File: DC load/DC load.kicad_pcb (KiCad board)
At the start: 2 copper layers, 100 x 88.9 mm, 26 parts, among them J1 CTL IN, J2 CTL OUT, J3 B+, J4 B-, M1 3.2mm, M2 3.2mm, M3 3.2mm, Q1 IRFI540, U1 LM324

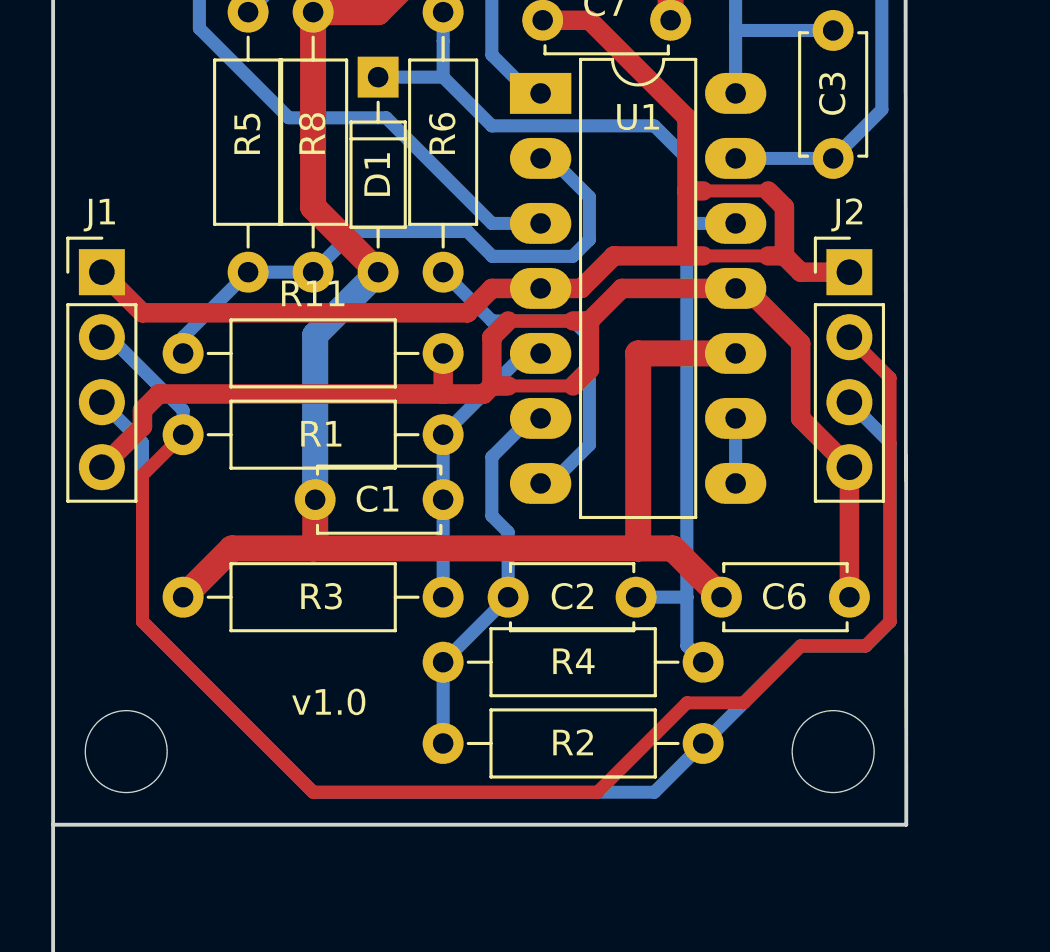
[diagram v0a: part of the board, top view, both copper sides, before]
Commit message: PCB layout - wider power tracks
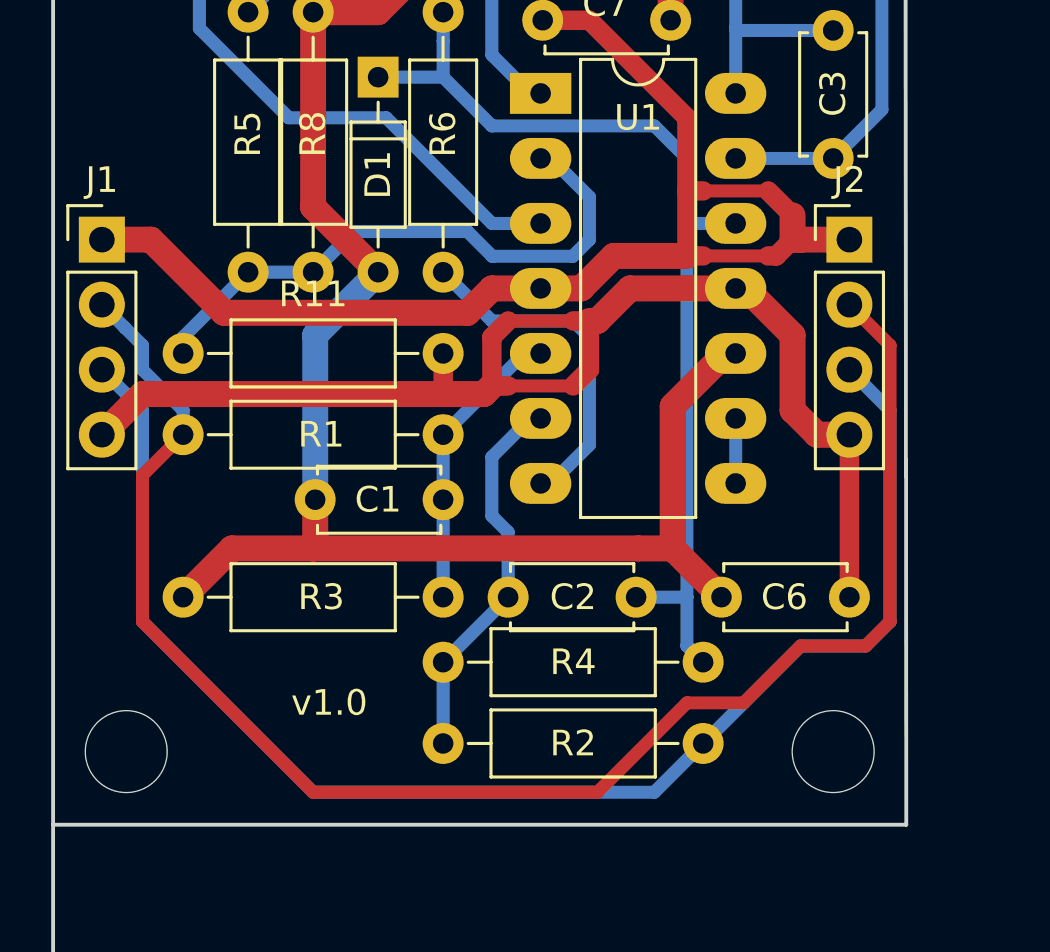
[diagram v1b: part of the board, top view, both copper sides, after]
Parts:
- moved J1 1.27 mm to (35.2, 54.9)
- moved J2 1.27 mm to (64.5, 54.9)
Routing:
- net GND: track 94.9 -> 92.3 mm
- net Net-(J1-Pad3): track 53.2 -> 55.7 mm
- net Net-(J1-Pad2): track 59.8 -> 62.1 mm

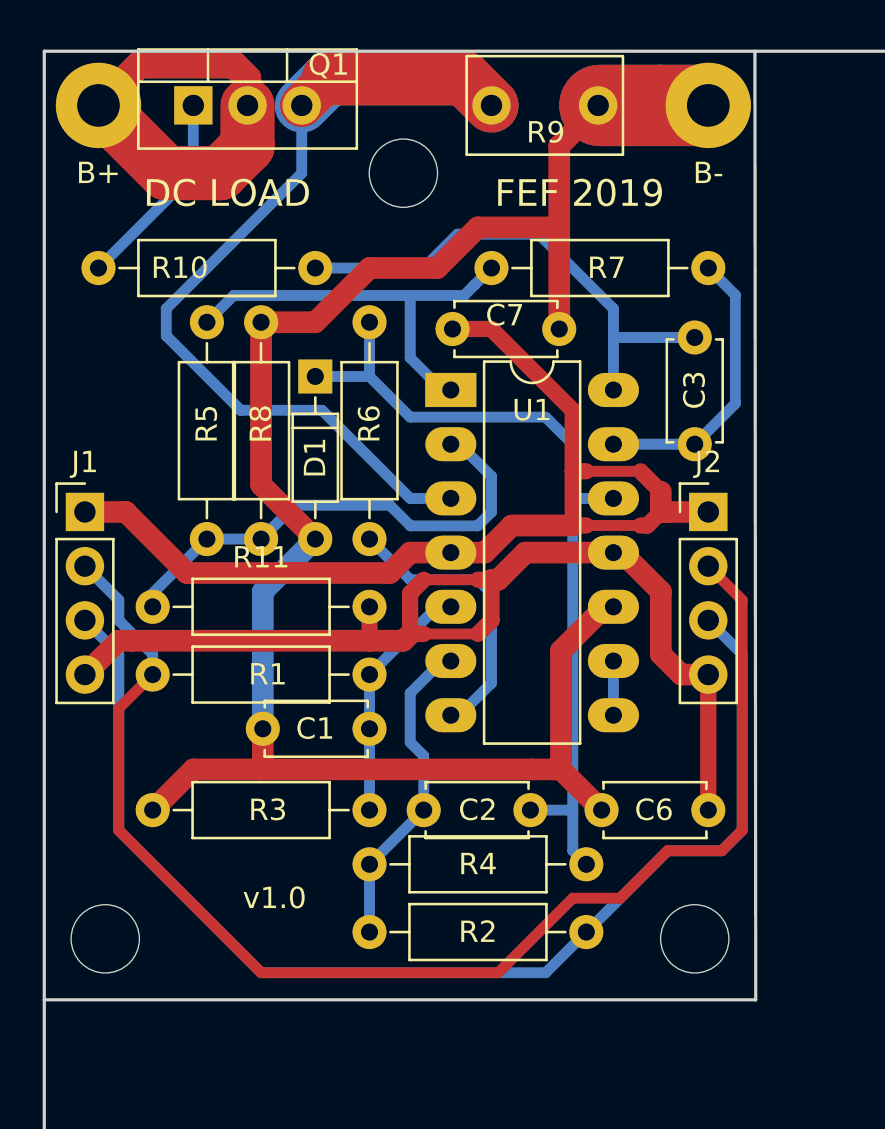
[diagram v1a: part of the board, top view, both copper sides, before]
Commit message: Some layout changes (smaller capacitor outlines; more space for connectors)
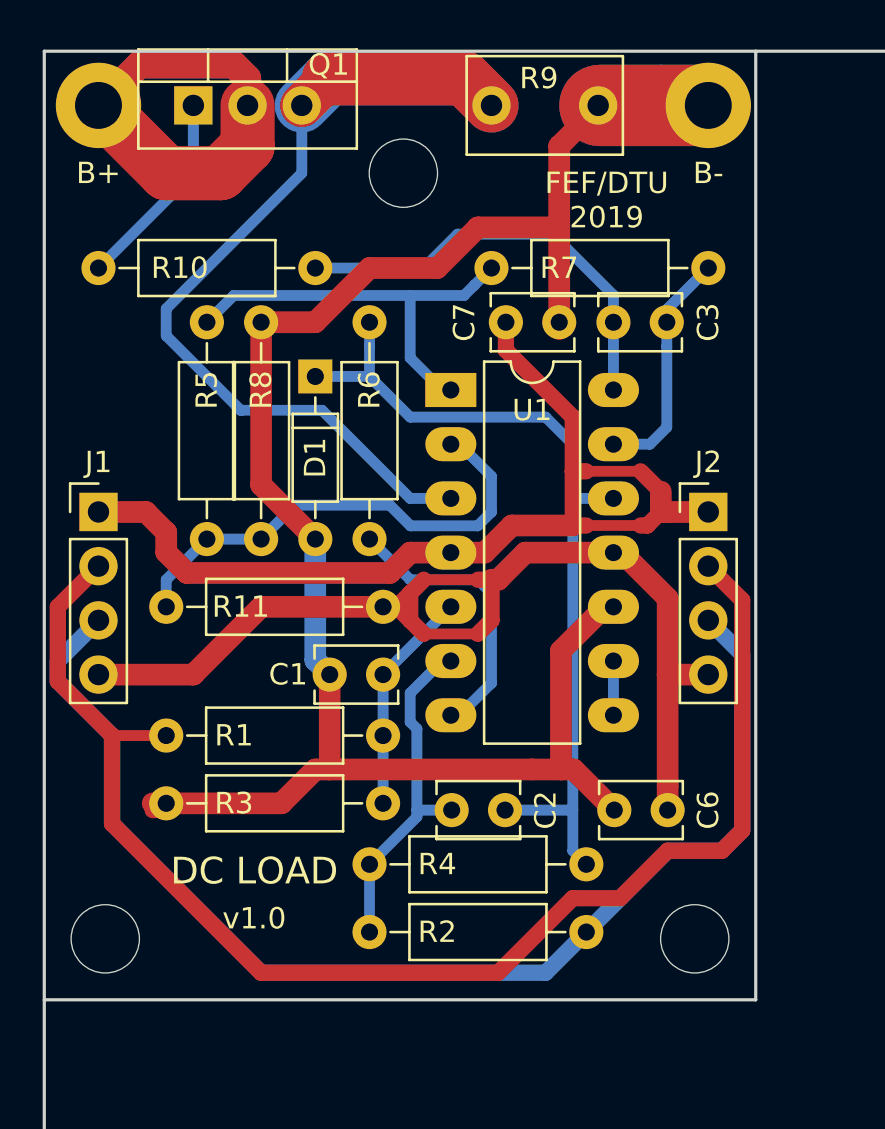
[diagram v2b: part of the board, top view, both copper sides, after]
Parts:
- C1, C2: value 1n -> 10n; footprint Capacitors_THT:C_Disc_D4.7mm_W2.5mm_P5.00mm -> Capacitors_THT:C_Disc_D3.8mm_W2.6mm_P2.50mm
- C3, C6, C7: footprint Capacitors_THT:C_Disc_D4.7mm_W2.5mm_P5.00mm -> Capacitors_THT:C_Disc_D3.8mm_W2.6mm_P2.50mm
- moved C1 4.03 mm to (46.7, 62.5)
- moved C3 3.88 mm to (60.0, 46.0), turned to 0 degrees
- moved R1 2.93 mm to (49.2, 65.4)
- moved C7 2.52 mm to (55.0, 46.0)
- moved C6 1.91 mm to (62.5, 68.9)
- moved C2 1.19 mm to (54.9, 68.9)
- moved R3 0.71 mm to (49.2, 68.6)
- moved R11 0.64 mm to (39.1, 59.4)
- moved J1 0.63 mm to (35.9, 54.9)
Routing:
- net Net-(C3-Pad1): track 23.7 -> 20.3 mm
- net VDD: track 49.7 -> 47.2 mm
- net Net-(C3-Pad2): track 13.4 -> 11.1 mm
- net Net-(J1-Pad2): track 62.1 -> 64.0 mm
- net Net-(C2-Pad2): track 15.0 -> 16.4 mm
- net Net-(J1-Pad3): track 55.7 -> 57.0 mm
- net Net-(C2-Pad1): track 40.2 -> 41.3 mm
- net Net-(C1-Pad2): track 11.5 -> 10.5 mm
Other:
- board text added: "FEF/DTU 2019"
- board text removed: "FEF 2019"

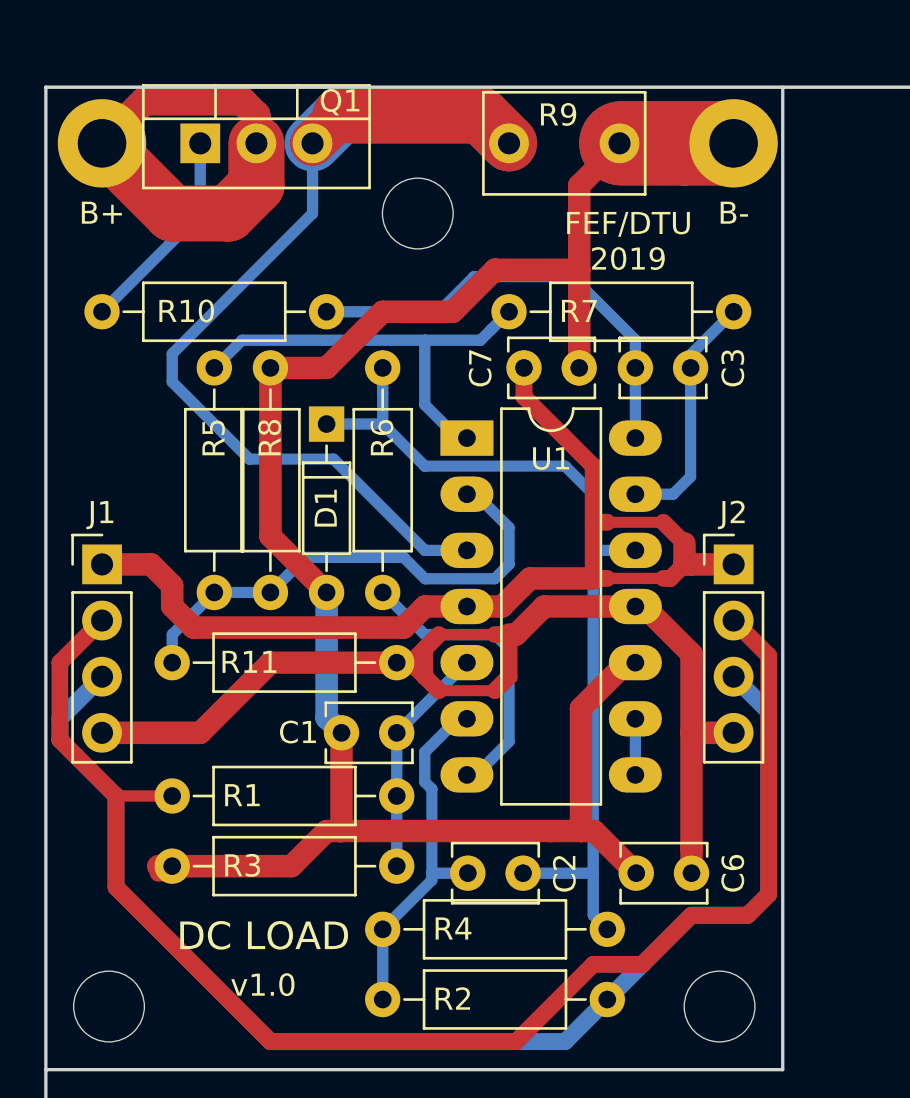
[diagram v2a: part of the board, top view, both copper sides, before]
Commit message: New TO247 housed FET for better dissipation
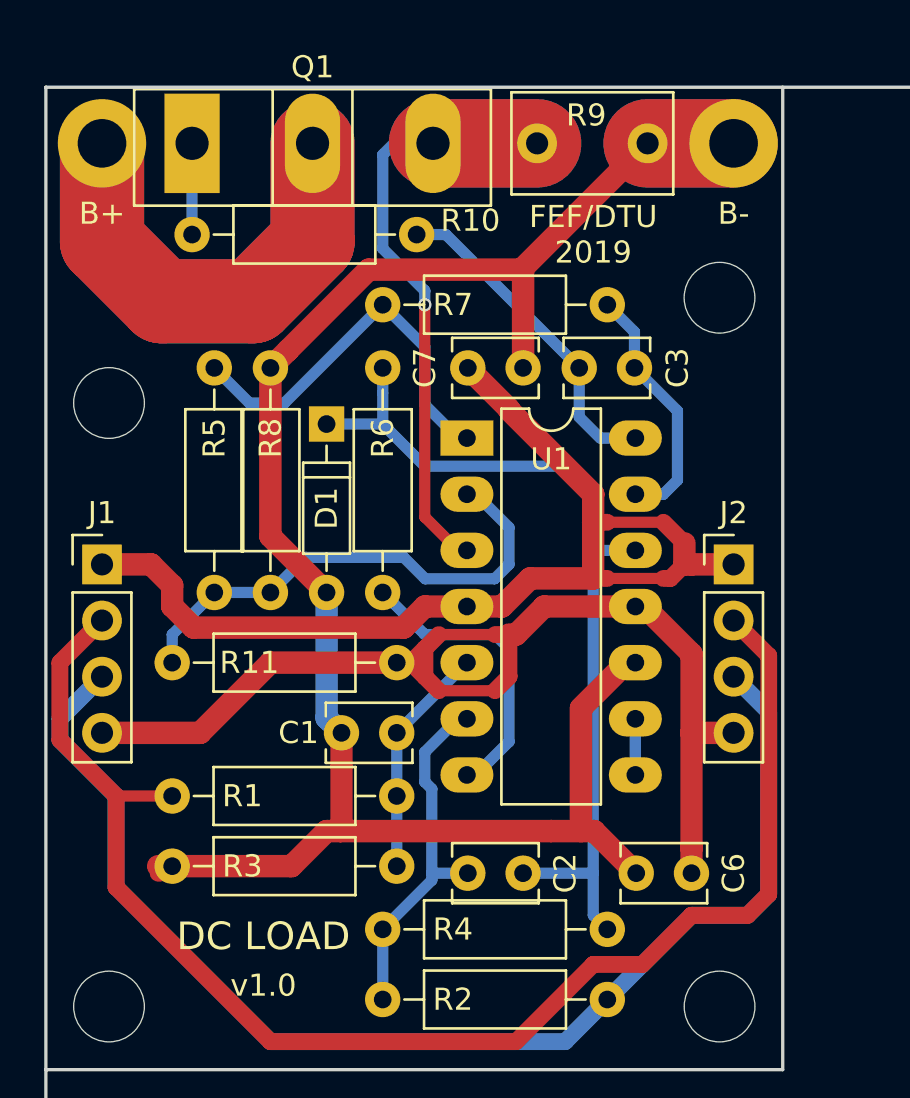
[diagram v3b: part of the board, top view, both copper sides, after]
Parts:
- added M1: 3.2mm, Mounting_Holes:MountingHole_3.2mm_M3_DIN965, F.Cu at (36.2, 47.6)
- Q1: value IRFI540 -> IRFP150NPBF; footprint TO_SOT_Packages_THT:TO-220-3_Vertical -> TO_SOT_Packages_THT:TO-247_TO-3P_Vertical
- moved M1 14.2 mm to (63.8, 42.9)
- moved R7 5.72 mm to (58.7, 43.2)
- moved R10 5.37 mm to (40.0, 40.0)
- moved C3 2.54 mm to (57.5, 46.0)
- moved C7 2.54 mm to (52.4, 46.0)
- moved R9 1.27 mm to (55.6, 35.9)
- moved Q1 0.37 mm to (40.0, 35.9)
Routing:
- net Net-(Q1-Pad3): track 50.2 -> 32.0 mm, vias 0 -> 1
- net Net-(J3-Pad1): track 29.3 -> 41.3 mm
- net Net-(Q1-Pad1): track 9.46 -> 4.13 mm
- net Net-(C3-Pad1): track 20.3 -> 15.0 mm
- net GND: track 92.0 -> 87.9 mm
- net Net-(R5-Pad1): track 20.2 -> 18.4 mm
- net VDD: track 47.2 -> 48.2 mm

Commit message: Layout fixes
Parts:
- renumbered M1 to M4
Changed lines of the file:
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@@
     (links 44)
     (no_connects 0)
-    (area 33.262499 33.262499 133.412501 122.312501)
+    (area 32.919999 31.4525 133.412501 122.312501)
     (thickness 1.6)
     (drawings 23)
@@
   )
   (setup
-    (last_trace_width 3.81)
+    (last_trace_width 0.25)
     (user_trace_width 0.254)
     (user_trace_width 0.381)
@@
     (tags "mounting hole 3.2mm no annular m3 din965")
     (attr virtual)
-    (fp_text reference M1 (at 0 -2.54) (layer F.SilkS) hide
+    (fp_text reference M4 (at 0 -2.54) (layer F.SilkS) hide
       (effects (font (size 1 1) (thickness 0.15)))
     )
@@
     (descr "C, Rect series, Radial, pin pitch=5.00mm, , length*width=7.2*4.5mm^2, Capacitor, http://www.wima.com/EN/WIMA_FKS_2.pdf")
     (tags "C Rect series Radial pin pitch 5.00mm  length 7.2mm width 4.5mm Capacitor")
-    (fp_text reference R9 (at 2.2225 -1.27) (layer F.SilkS)
+    (fp_text reference R9 (at 2.54 -1.5875) (layer F.SilkS)
       (effects (font (size 1 1) (thickness 0.15)))
     )
@@
     (fp_line (start 6.45 2.6) (end 6.45 -2.6) (layer F.CrtYd) (width 0.05))
     (fp_line (start 6.45 -2.6) (end -1.45 -2.6) (layer F.CrtYd) (width 0.05))
-    (fp_text user %R (at 2.2225 -1.27) (layer F.Fab)
+    (fp_text user %R (at 2.54 -1.5875) (layer F.Fab)
       (effects (font (size 1 1) (thickness 0.15)))
     )
@@
     (descr "TO-247, Vertical, RM 5.45mm, TO-3P")
     (tags "TO-247 Vertical RM 5.45mm TO-3P")
-    (fp_text reference Q1 (at 5.45 -3.45) (layer F.SilkS)
+    (fp_text reference Q1 (at 8.625 1.905) (layer F.SilkS)
       (effects (font (size 1 1) (thickness 0.15)))
     )
@@
       (effects (font (size 1 1) (thickness 0.15)))
     )
-    (fp_text user %R (at 5.45 -3.45) (layer F.Fab)
-      (effects (font (size 1 1) (thickness 0.15)))
-    )
+    (fp_text user %R (at 8.625 1.905) (layer F.Fab)
+      (effects (font (size 1 1) (thickness 0.15)))
+    )

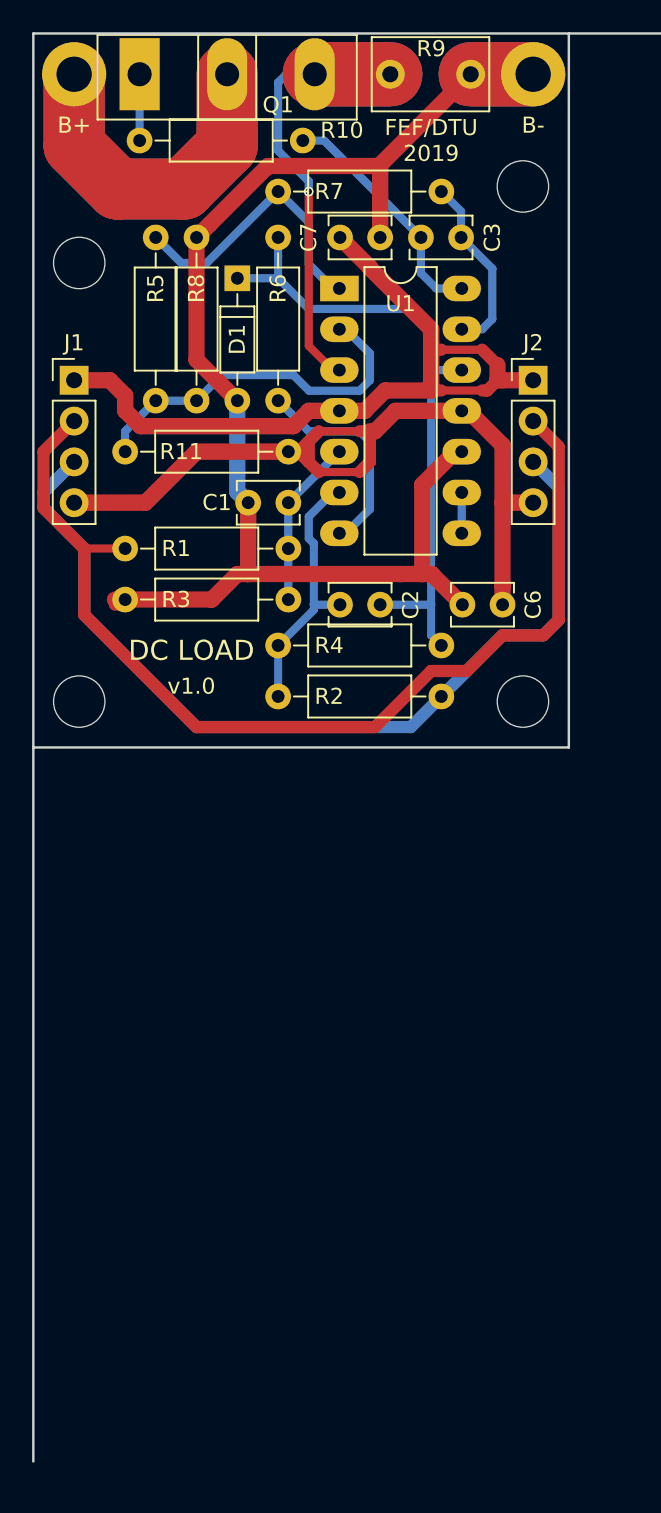
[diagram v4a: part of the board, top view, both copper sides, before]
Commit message: Controller enhancements
Safety relay control
Input polarity check
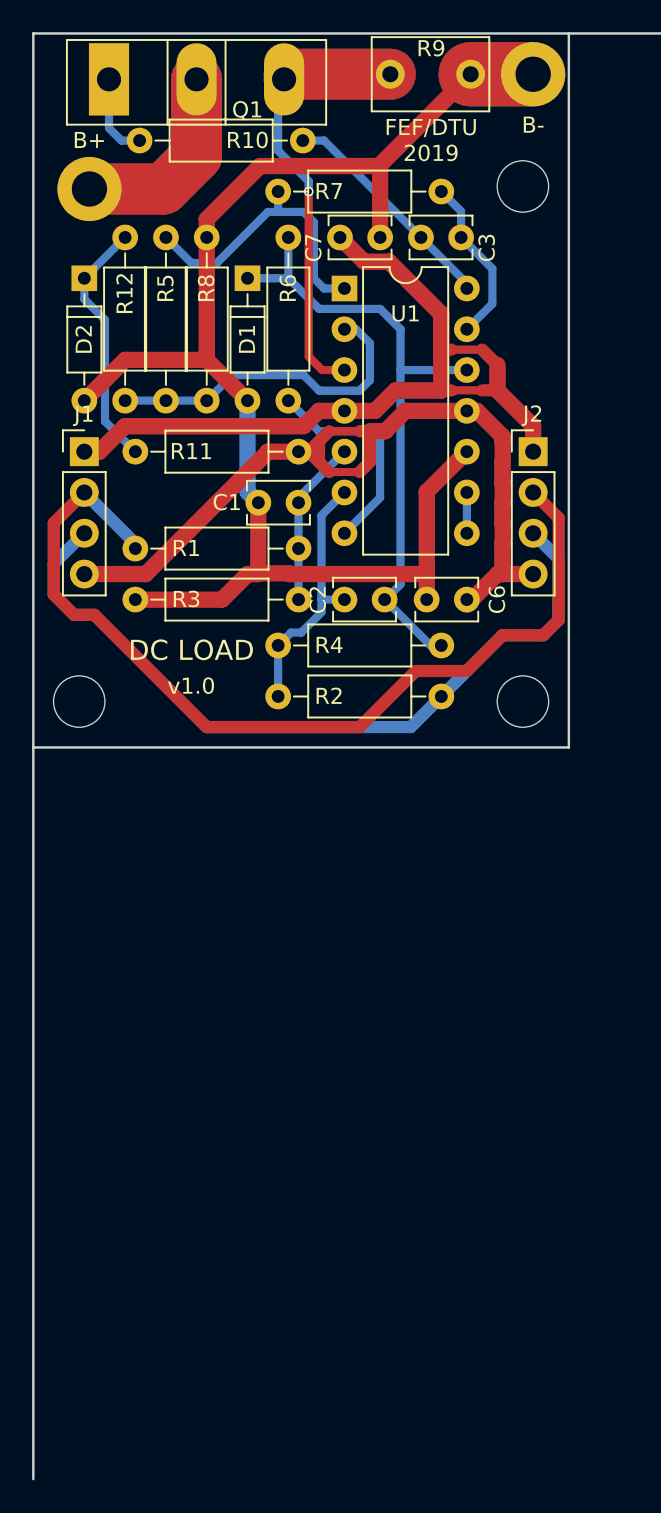
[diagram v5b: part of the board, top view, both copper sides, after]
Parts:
- removed M1: 3.2mm, Mounting_Holes:MountingHole_3.2mm_M3_DIN965
- added D2: 1n4148, Diodes_THT:D_DO-35_SOD27_P7.62mm_Horizontal, F.Cu at (36.5, 48.6)
- added R12: 127k, Resistors_THT:R_Axial_DIN0207_L6.3mm_D2.5mm_P10.16mm_Horizontal, F.Cu at (39.1, 56.2)
- R11: value 2M2 -> 11k5
- U1: footprint Housings_DIP:DIP-14_W7.62mm_LongPads -> Housings_DIP:DIP-14_W7.62mm
- moved J3 7.21 mm to (36.8, 43.0)
- moved J1 4.49 mm to (36.5, 59.4)
- moved J2 4.45 mm to (64.5, 59.4)
- moved C6 2.25 mm to (60.3, 68.6)
- moved Q1 1.93 mm to (38.0, 36.2)
- moved C1 0.63 mm to (47.3, 62.5)
- moved D1 0.63 mm to (46.7, 48.6)
- moved R1 0.63 mm to (49.8, 65.4)
- moved R11 0.63 mm to (39.7, 59.4)
- moved R3 0.63 mm to (49.8, 68.6)
- moved R5 0.63 mm to (41.6, 46.0)
- moved R6 0.63 mm to (49.2, 56.2)
- moved R8 0.63 mm to (44.1, 56.2)
- moved C2 0.42 mm to (55.2, 68.6)
- moved U1 0.32 mm to (52.7, 49.2)
- renumbered M4 to M3
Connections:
- R11 pad 1: Net-(R11-Pad1) -> Net-(D2-Pad1)
- R5 pad 2: Net-(R11-Pad1) -> Net-(R12-Pad1)
- R8 pad 1: Net-(R11-Pad1) -> Net-(R12-Pad1)
- U1 pad 2: Net-(R11-Pad1) -> Net-(R12-Pad1)
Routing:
- net Net-(R11-Pad1): track 23.2 -> 0.00 mm
- net Net-(R12-Pad1): track 0.00 -> 20.8 mm
- net Net-(J3-Pad1): track 41.3 -> 24.6 mm
- net Net-(D2-Pad1): track 0.00 -> 15.7 mm
- net Net-(J1-Pad3): track 57.0 -> 48.3 mm
- net Net-(J1-Pad2): track 64.0 -> 58.2 mm
- net GND: track 87.9 -> 93.6 mm
- net Net-(Q1-Pad3): track 32.0 -> 34.7 mm
- net VDD: track 48.2 -> 50.5 mm
- net VSS: track 50.4 -> 52.4 mm
- net Net-(C2-Pad1): track 41.3 -> 39.4 mm
- net Net-(Q1-Pad1): track 4.13 -> 5.26 mm
- net Net-(C3-Pad2): track 11.4 -> 10.5 mm
- net Net-(C3-Pad1): track 15.0 -> 14.2 mm
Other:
- board size 100 x 88.9 mm -> 100 x 90 mm
